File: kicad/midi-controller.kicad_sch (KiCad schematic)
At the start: 39 parts, among them J16 Conn_01x06_Socket, J2 Conn_02x03_Counter_Clockwise, J35 Conn_01x06_Socket, J37 Conn_01x06_Socket, J38 Conn_01x06_Socket, J39 Conn_01x06_Socket, J8 Conn_01x07_Socket, U1 RP2040, U2 AT25SF081-SSHD-X, U35 ESP32-WROOM-32U, U6 MCP23S17_SO, U8 LM4040D33, Y1 12Mhz

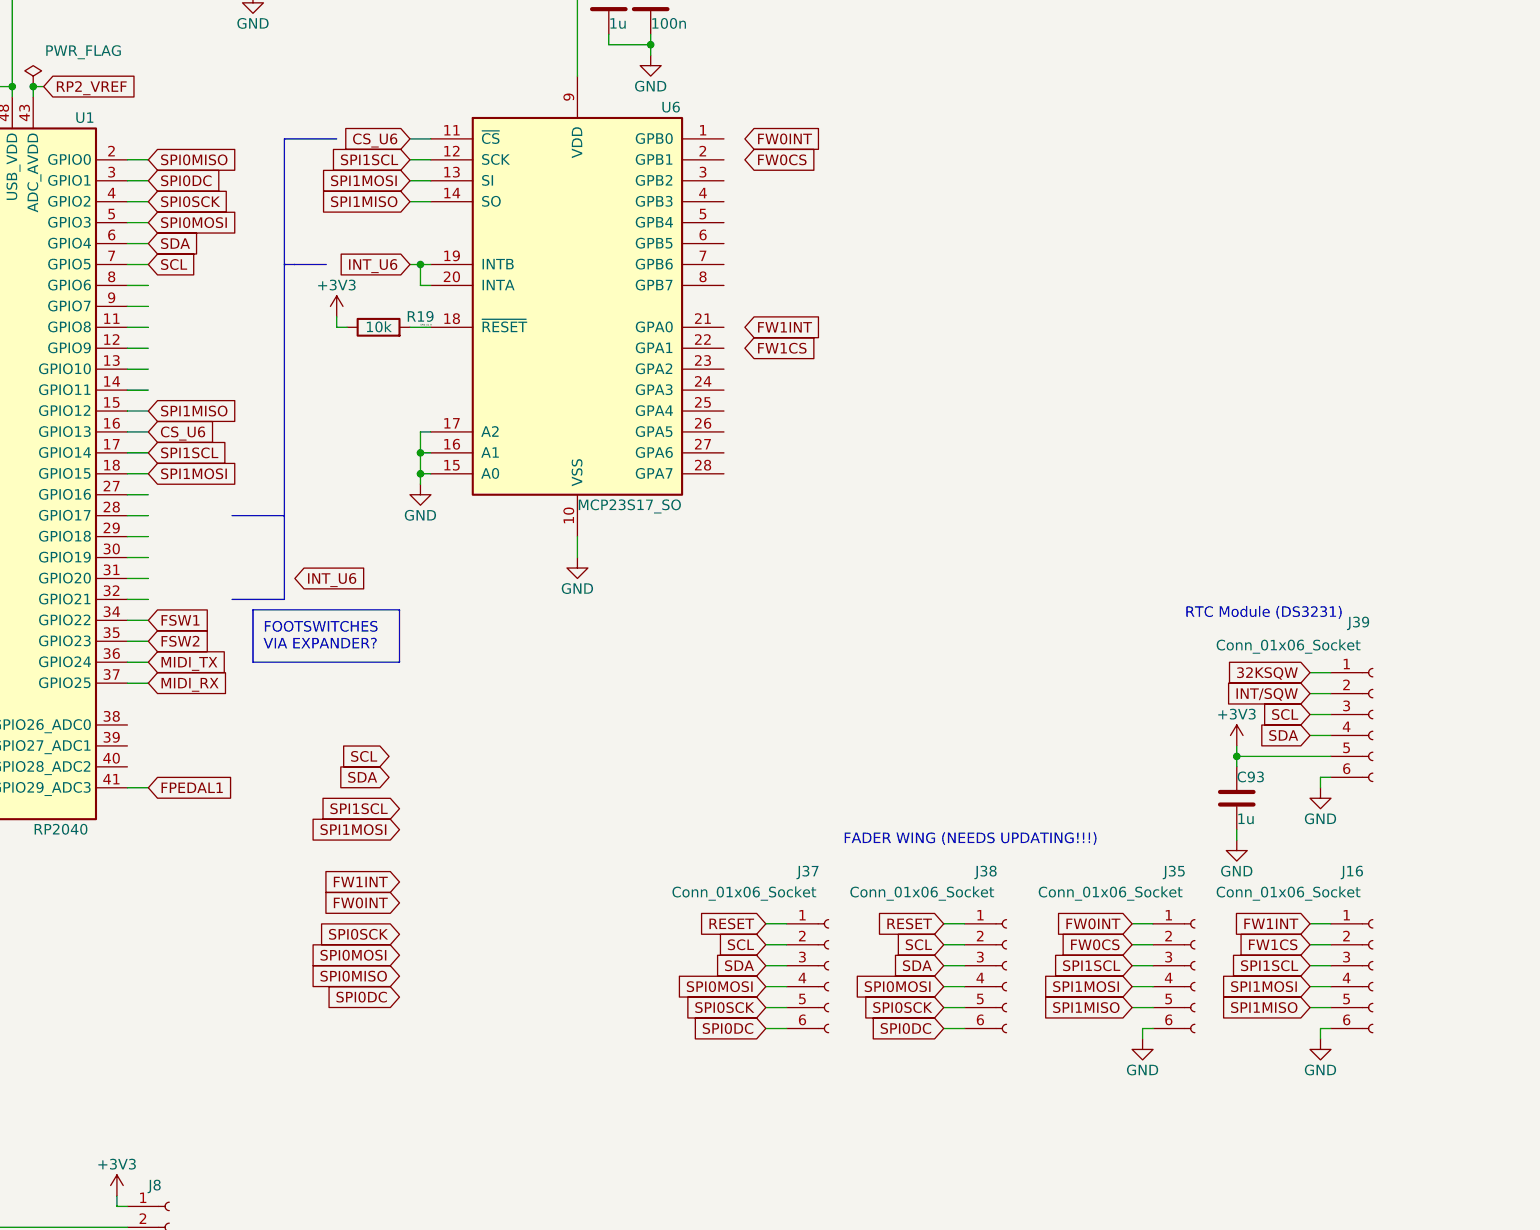
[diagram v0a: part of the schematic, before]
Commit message: feat(schem): started implementing the rp2040 on each wing
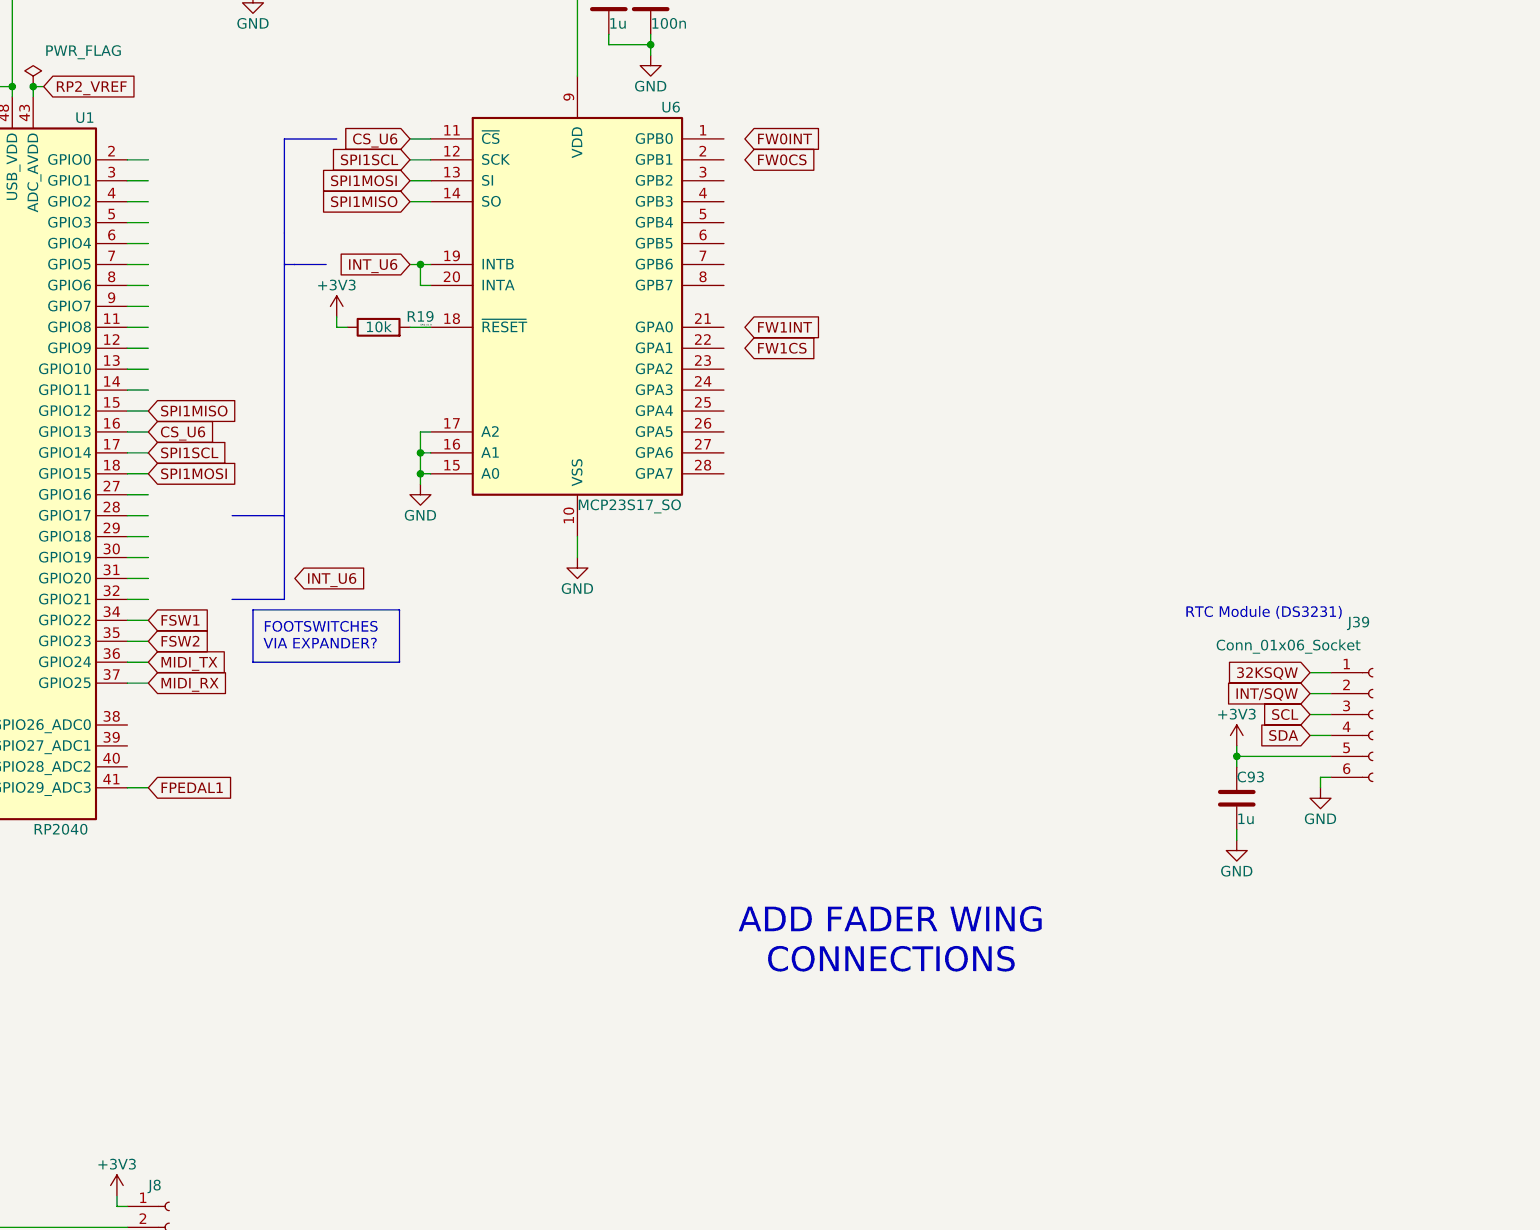
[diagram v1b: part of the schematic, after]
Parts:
- removed J16, J35, J37, J38: Conn_01x06_Socket, Connector_JST:JST_XH_B6B-XH-A_1x06_P2.50mm_Vertical, symbol Connector:Conn_01x06_Socket
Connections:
- net SCL: no longer U1.7 (GPIO5)
- net SDA: no longer U1.6 (GPIO4)
- net SPI0DC: no longer names the net of U1.3 (GPIO1)
- net SPI0MISO: no longer names the net of U1.2 (GPIO0)
- net SPI0MOSI: no longer names the net of U1.5 (GPIO3)
- net SPI0SCK: no longer names the net of U1.4 (GPIO2)
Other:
- note added: "ADD FADER WING CONNECTIONS"
- note removed: "FADER WING (NEEDS UPDATING!!!)"

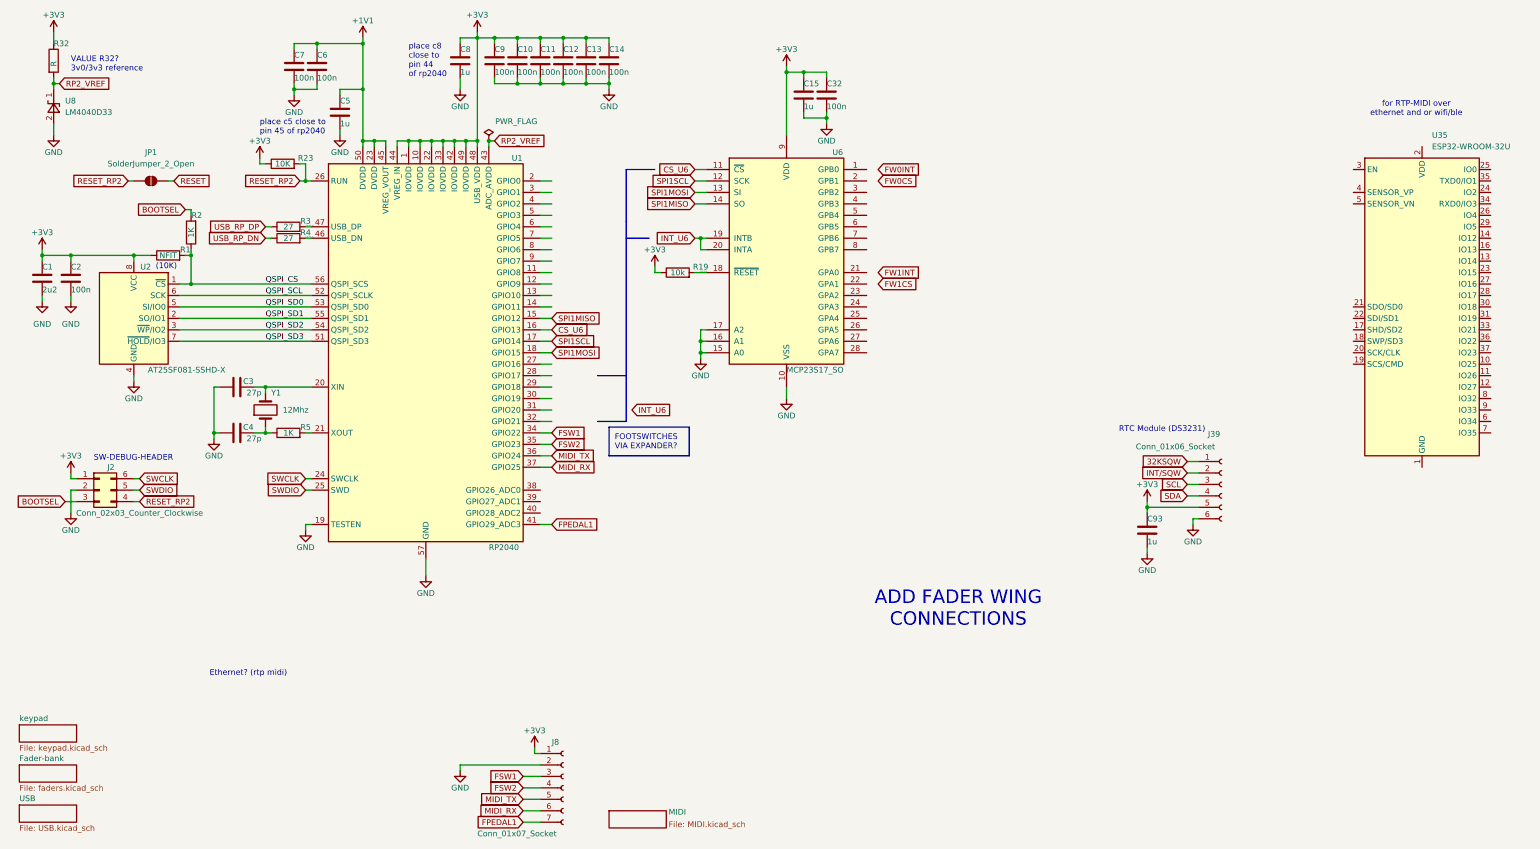
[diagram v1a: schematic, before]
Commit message: continued work on fader pcb and redid all references more logicly
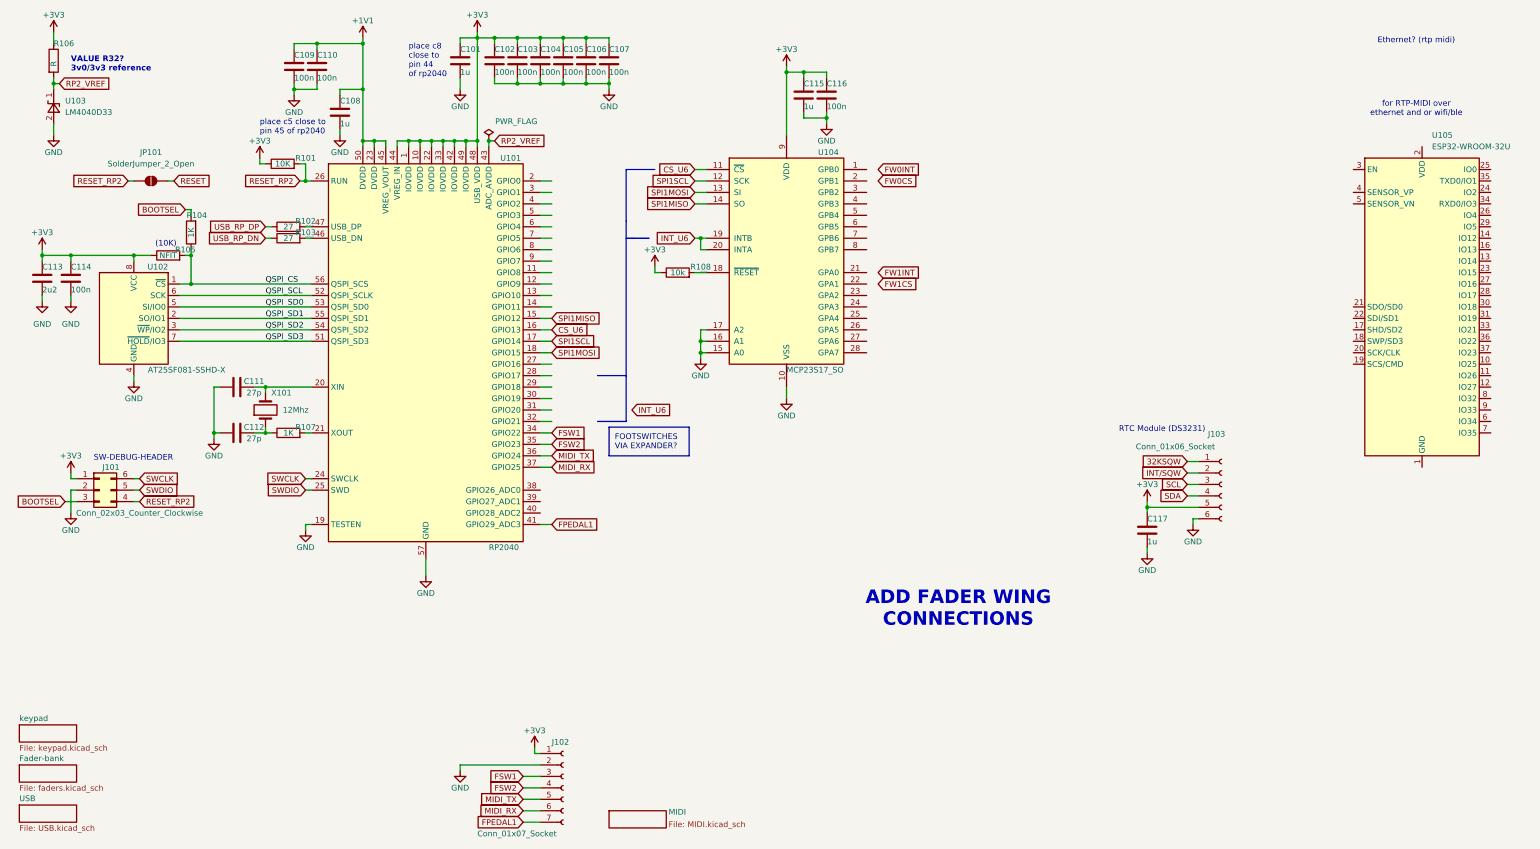
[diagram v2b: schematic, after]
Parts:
- renumbered C8 to C101, C9 to C102, C10 to C103, C11 to C104, C12 to C105, C13 to C106, C14 to C107, C5 to C108, C7 to C109, C6 to C110, C3 to C111, C4 to C112, C1 to C113, C2 to C114, C15 to C115, C32 to C116, C93 to C117, J2 to J101, J8 to J102, J39 to J103, JP1 to JP101, R23 to R101, R3 to R102, R4 to R103, R2 to R104, R1 to R105, R32 to R106, R5 to R107, R19 to R108, U1 to U101, U2 to U102, U8 to U103, U6 to U104, U35 to U105, Y1 to X101
